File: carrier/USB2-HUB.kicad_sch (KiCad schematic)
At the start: 34 parts, among them J2 USB_C_Receptacle_USB2.0, J3 Conn_02x04, J4 690-008-221-904, U2 AP22653W6, U3 USB2514B-I/M2, U4 FSUSB42MUX, U5 TPD4EUSB30, Y1 24MHz

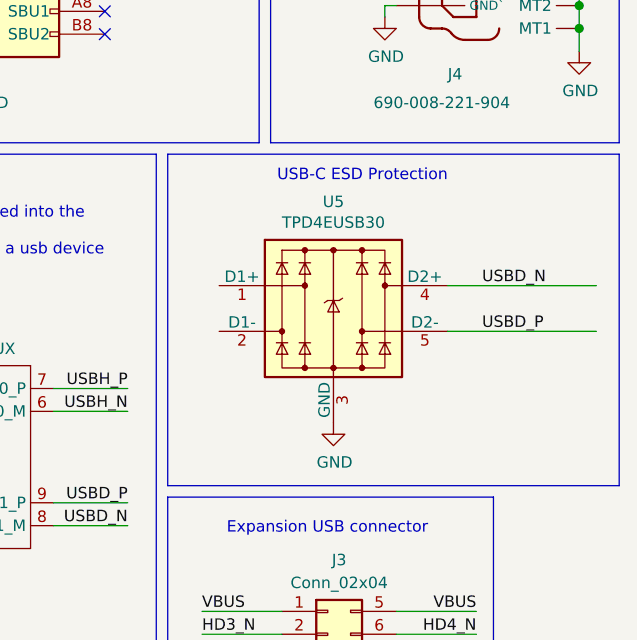
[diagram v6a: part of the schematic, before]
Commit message: Feat: routed differential pairs. 90 more routes to go
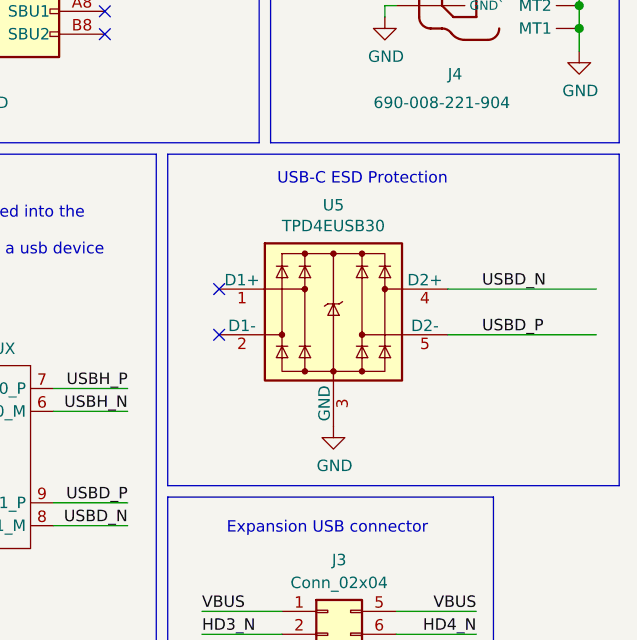
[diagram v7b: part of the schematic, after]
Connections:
- no-connect marks 9 -> 11
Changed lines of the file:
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@@
   (no_connect (at 87.122 146.812))
   (no_connect (at 87.122 144.272))
+  (no_connect (at 233.68 96.266))
   (no_connect (at 87.122 126.492))
   (no_connect (at 220.98 60.325))
   (no_connect (at 143.002 141.732))
   (no_connect (at 198.12 70.485))
+  (no_connect (at 233.68 91.186))
   (no_connect (at 143.002 129.032))
   (wire (pts (xy 85.852 111.252) (xy 85.852 96.012))
@@
     (stroke (width 0) (type solid))
   )
-  (wire (pts (xy 259.08 90.805) (xy 275.59 90.805))
+  (wire (pts (xy 259.08 91.186) (xy 275.59 91.186))
     (stroke (width 0) (type solid))
   )
@@
     (stroke (width 0) (type solid))
   )
-  (wire (pts (xy 259.08 95.885) (xy 275.59 95.885))
+  (wire (pts (xy 259.08 96.266) (xy 275.59 96.266))
     (stroke (width 0) (type solid))
   )
@@
   )
   (text "USB-C ESD Protection" (exclude_from_sim no)
- (at 259.08 79.375 0)
+ (at 259.08 79.756 0)
     (effects (font (size 1.27 1.27)) (justify right bottom))
   )
@@
     (effects (font (size 1.27 1.27)) (justify left bottom))
   )
-  (label "USBD_P" (at 262.89 95.885 0) (fields_autoplaced)
+  (label "USBD_P" (at 262.89 96.266 0) (fields_autoplaced)
     (effects (font (size 1.27 1.27)) (justify left bottom))
   )
@@
     (effects (font (size 1.27 1.27)) (justify left bottom))
   )
-  (label "USBD_N" (at 262.89 90.805 0) (fields_autoplaced)
+  (label "USBD_N" (at 262.89 91.186 0) (fields_autoplaced)
     (effects (font (size 1.27 1.27)) (justify left bottom))
   )
@@
     )
   )
-  (symbol (lib_id "power:GND") (at 246.38 106.045 0) (unit 1)
-    (in_bom yes) (on_board yes) (dnp no)
-    (property "Reference" "#PWR028" (at 246.38 112.395 0)
-      (effects (font (size 1.27 1.27)) hide)
-    )
-    (property "Value" "GND" (at 246.507 110.4392 0)
-      (effects (font (size 1.27 1.27)))
-    )
-    (property "Footprint" "" (at 246.38 106.045 0)
-      (effects (font (size 1.27 1.27)) hide)
-    )
-    (property "Datasheet" "" (at 246.38 106.045 0)
+  (symbol (lib_id "power:GND") (at 246.38 106.426 0) (unit 1)
+    (in_bom yes) (on_board yes) (dnp no)
+    (property "Reference" "#PWR028" (at 246.38 112.776 0)
+      (effects (font (size 1.27 1.27)) hide)
+    )
+    (property "Value" "GND" (at 246.507 110.8202 0)
+      (effects (font (size 1.27 1.27)))
+    )
+    (property "Footprint" "" (at 246.38 106.426 0)
+      (effects (font (size 1.27 1.27)) hide)
+    )
+    (property "Datasheet" "" (at 246.38 106.426 0)
       (effects (font (size 1.27 1.27)) hide)
     )
@@
     )
   )
-  (symbol (lib_id "CM4IO:TPD4EUSB30") (at 246.38 93.345 0) (unit 1)
-    (in_bom yes) (on_board yes) (dnp no)
-    (property "Reference" "U5" (at 246.38 81.4832 0)
-      (effects (font (size 1.27 1.27)))
-    )
-    (property "Value" "TPD4EUSB30" (at 246.38 83.7946 0)
-      (effects (font (size 1.27 1.27)))
-    )
-    (property "Footprint" "Package_SON:USON-10_2.5x1.0mm_P0.5mm" (at 222.25 103.505 0)
-      (effects (font (size 1.27 1.27)) hide)
-    )
-    (property "Datasheet" "http://www.ti.com/lit/ds/symlink/tpd2eusb30a.pdf" (at 246.38 93.345 0)
-      (effects (font (size 1.27 1.27)) hide)
-    )
-    (property "Field4" "Farnell" (at 246.38 93.345 0)
-      (effects (font (size 1.27 1.27)) hide)
-    )
-    (property "Field5" "2335455" (at 246.38 93.345 0)
-      (effects (font (size 1.27 1.27)) hide)
-    )
-    (property "Field6" "CDDFN10-3324P-13" (at 246.38 93.345 0)
-      (effects (font (size 1.27 1.27)) hide)
-    )
-    (property "Field7" "Bourns" (at 246.38 93.345 0)
-      (effects (font (size 1.27 1.27)) hide)
-    )
-    (property "Field8" "UDIO00346" (at 246.38 93.345 0)
-      (effects (font (size 1.27 1.27)) hide)
-    )
-    (property "Part Description" "Quad TVS diode for high speed signals (USB3, GigE etc.)" (at 246.38 93.345 0)
-      (effects (font (size 1.27 1.27)) hide)
-    )
+  (symbol (lib_id "CM4IO:TPD4EUSB30") (at 246.38 93.726 0) (unit 1)
+    (in_bom yes) (on_board yes) (dnp no)
+    (property "Reference" "U5" (at 246.38 81.8642 0)
+      (effects (font (size 1.27 1.27)))
+    )
+    (property "Value" "TPD4EUSB30" (at 246.38 84.1756 0)
+      (effects (font (size 1.27 1.27)))
+    )
+    (property "Footprint" "Package_SON:USON-10_2.5x1.0mm_P0.5mm" (at 222.25 103.886 0)
+      (effects (font (size 1.27 1.27)) hide)
+    )
+    (property "Datasheet" "http://www.ti.com/lit/ds/symlink/tpd2eusb30a.pdf" (at 246.38 93.726 0)
+      (effects (font (size 1.27 1.27)) hide)
+    )
+    (property "Field4" "Farnell" (at 246.38 93.726 0)
+      (effects (font (size 1.27 1.27)) hide)
+    )
+    (property "Field5" "2335455" (at 246.38 93.726 0)
+      (effects (font (size 1.27 1.27)) hide)
+    )
+    (property "Field6" "CDDFN10-3324P-13" (at 246.38 93.726 0)
+      (effects (font (size 1.27 1.27)) hide)
+    )
+    (property "Field7" "Bourns" (at 246.38 93.726 0)
+      (effects (font (size 1.27 1.27)) hide)
+    )
+    (property "Field8" "UDIO00346" (at 246.38 93.726 0)
+      (effects (font (size 1.27 1.27)) hide)
+    )
+    (property "Part Description" "Quad TVS diode for high speed signals (USB3, GigE etc.)" (at 246.38 93.726 0)
+      (effects (font (size 1.27 1.27)) hide)
+    )

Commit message: Feat: all traces routed
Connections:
- net GND: now also J2.S1 (SHIELD)
- no-connect marks 11 -> 10
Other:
- moved on the sheet: J2, R11, R12
